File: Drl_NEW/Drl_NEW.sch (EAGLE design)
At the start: 23 parts, among them IC1 TINY13-20SSU, IC2 78L05, Q1 IRF7240PBF, Q2 IRF7240PBF, X1 PROG-ISP6POGOPIN

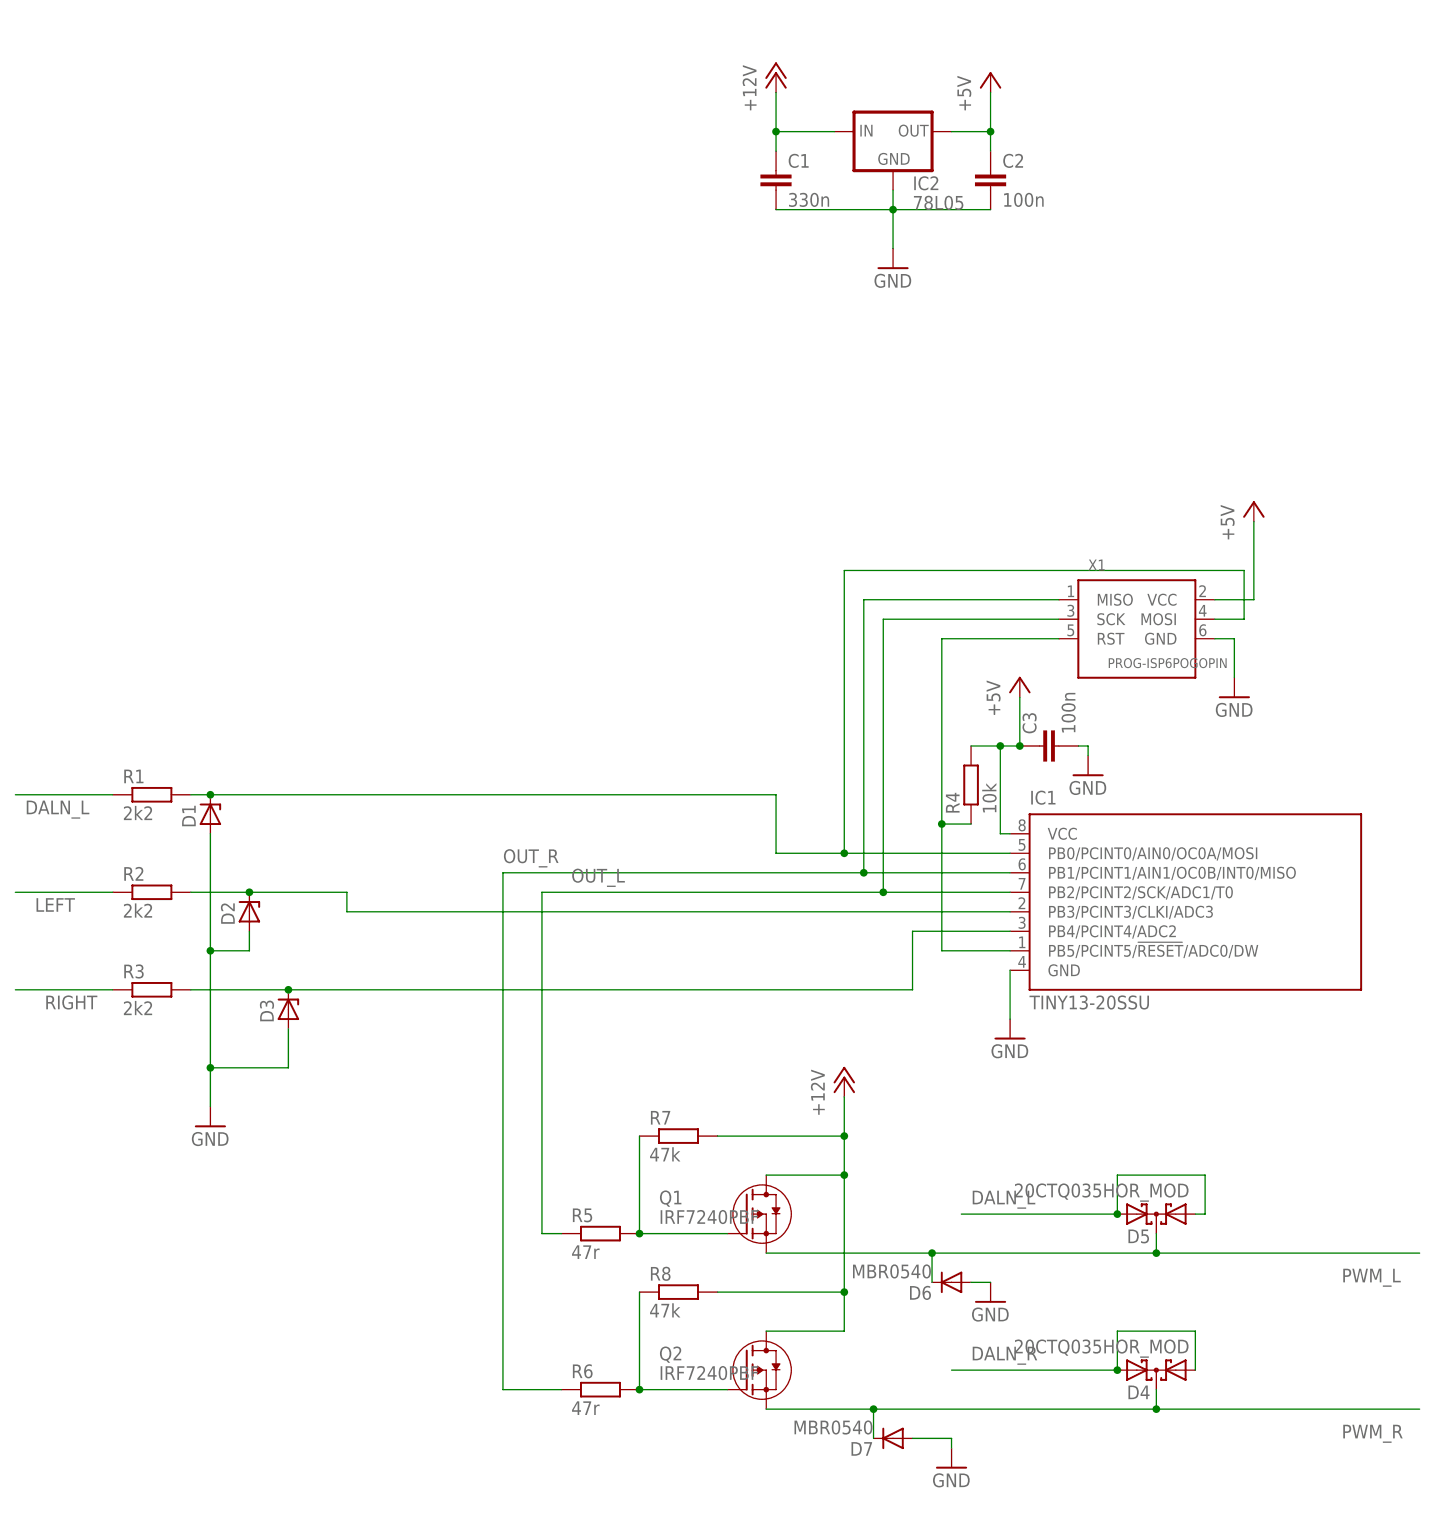
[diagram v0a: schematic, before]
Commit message: Добавлены ДХО работающие на ШИМ
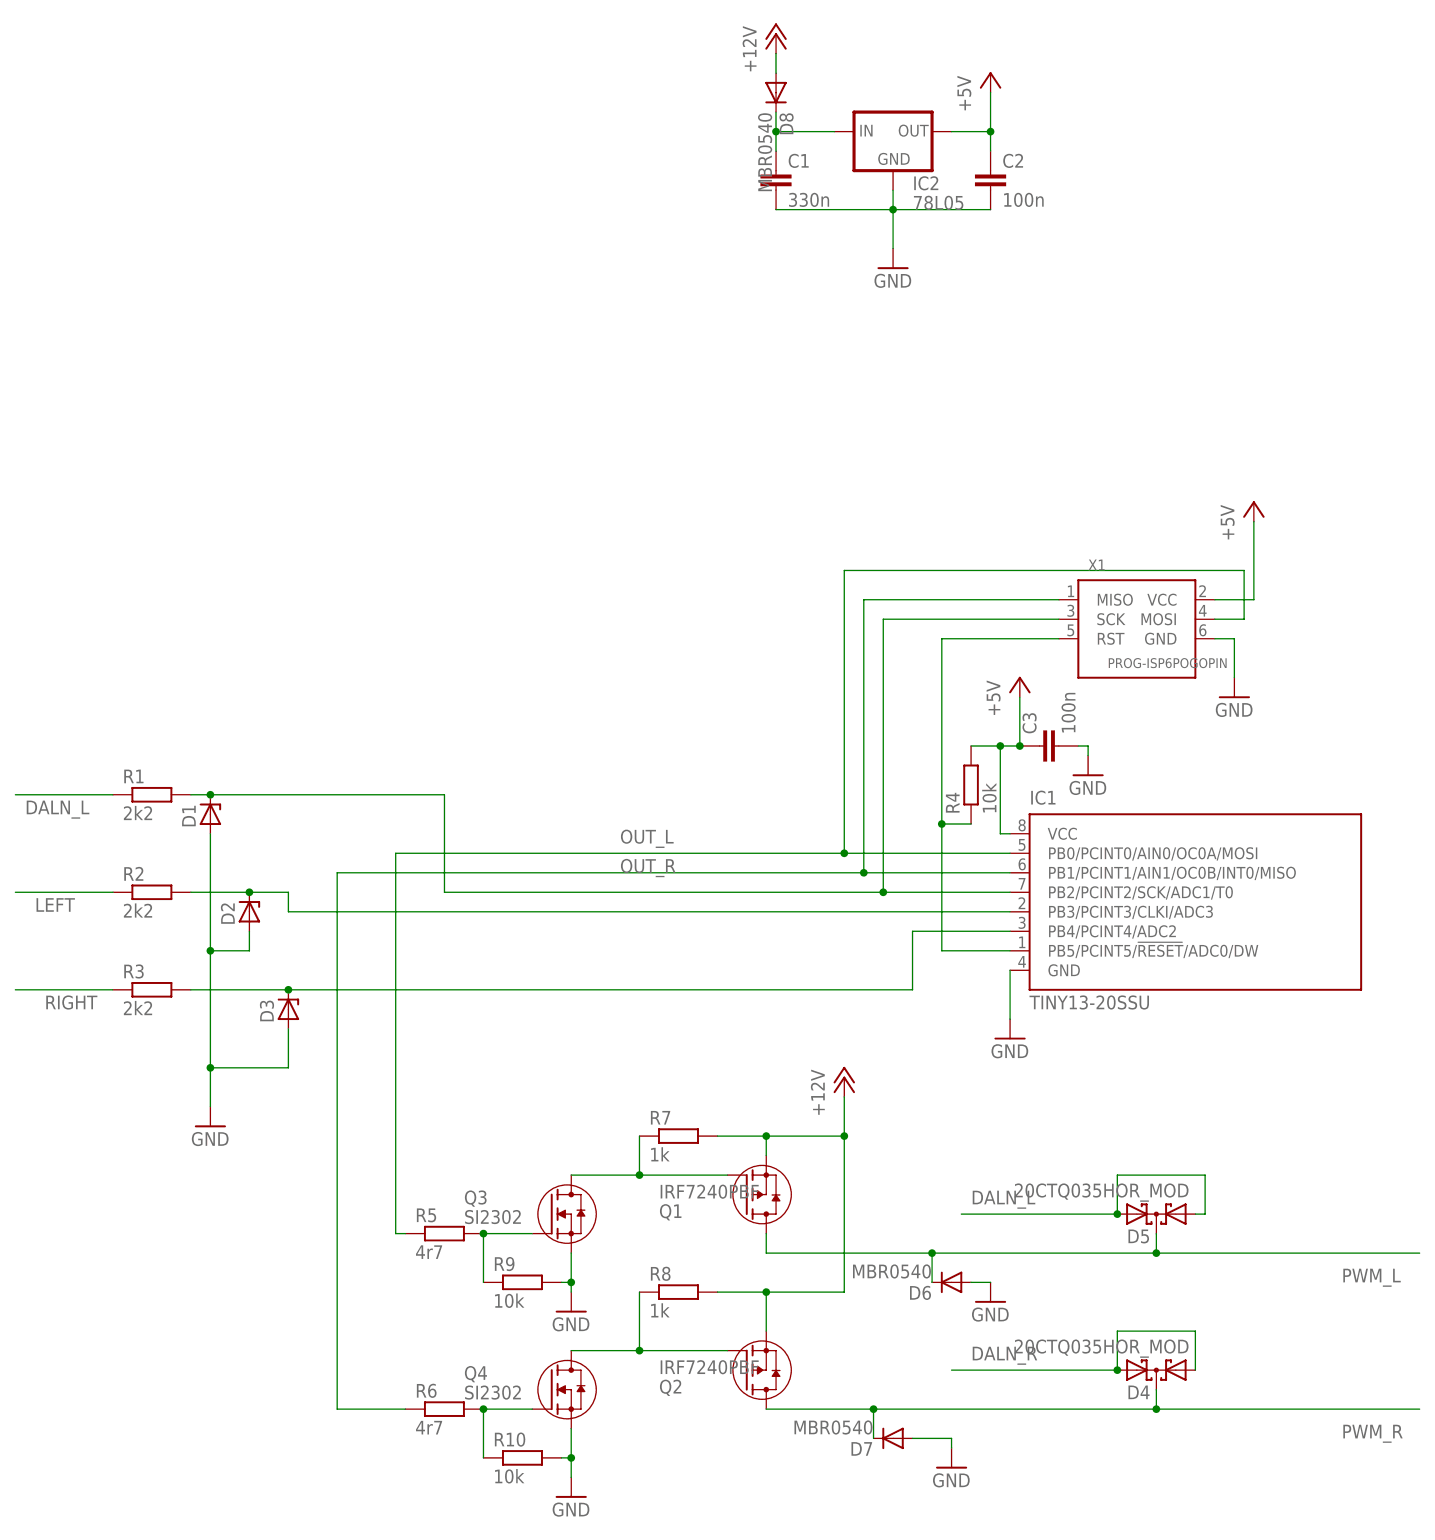
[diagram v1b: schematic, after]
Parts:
- added D8: MBR0540, diode:CGRM4001-G
- added Q3, Q4: SI2302, usb:SI2302
- added R10, R9: 10k, rcl:R-EU_R0603
- IC2: device usb:78LXX -> usb:78LXXSOT89
- R5, R6: value 47r -> 4r7
- R7, R8: value 47k -> 1k
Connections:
- new net N$11: Q3.G, R5.2, R9.1
- new net N$12: Q4.G, R10.1, R6.2
- new net N$13: D1.C, IC1.PB2/PCINT2/SCK/ADC1/T0, R1.2, X1.SCK
- net +12V: now also D8.A, Q1.S, Q2.S; no longer C1.1, IC2.IN, Q1.D, Q2.D
- net GND: now also Q3.S, Q4.S, R10.2, R9.2
- net N$4: now also Q4.D; no longer R6.2
- net N$6: now also C1.1, D8.C, IC2.IN; no longer D1.C, IC1.PB0/PCINT0/AIN0/OC0A/MOSI, R1.2, X1.MOSI
- net N$8: now also Q3.D; no longer R5.2
- net OUT_L: now also IC1.PB0/PCINT0/AIN0/OC0A/MOSI, X1.MOSI; no longer IC1.PB2/PCINT2/SCK/ADC1/T0, X1.SCK
- net PWM_L: now also Q1.D; no longer Q1.S
- net PWM_R: now also Q2.D; no longer Q2.S
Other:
- moved on the sheet: Q1, Q2, R5, R6
